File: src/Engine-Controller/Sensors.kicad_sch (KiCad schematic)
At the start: 28 parts, among them P16 647676-2, P17 0530470410, P8 20021511-00026T4LF, U12 MAX4617EUE+T, U13 MAX4617EUE+T, U14 MCP96L01T-E_MX, U15 AD623ARZ-R7, U7 MC74HC4066ADG, U8 AD623ARZ-R7, U9 MC74HC4066ADG

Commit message: resolved all ERC schematic issues
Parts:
- C32: footprint (none) -> Engine-Controller:CAP_0603
- P16: footprint CONN_2043-1X04G00DAU_OUP -> Engine-Controller:647676-2
- P17: footprint CONN_4840.2201_SCH -> Engine-Controller:0530470410
- P8: footprint CONN20_D10-RA-BK_SUL -> Engine-Controller:20021511-00026T4LF
- R19, R20, R21, R22, R23, R24, R25, R26, R27, R29, R30, R31, R32: footprint (none) -> Engine-Controller:RES_0603
- R33: footprint (none) -> Engine-Controller:RES_0805
- U12, U13: footprint (none) -> Engine-Controller:max4617eue
- U14: footprint (none) -> Engine-Controller:MCP96L01T-E_MX
- U15, U8: footprint R_8_ADI -> Engine-Controller:AD623ARZ-R7
- U7, U9: footprint (none) -> Engine-Controller:MC74HC4066ADG
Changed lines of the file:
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@@
       (effects (font (size 1.27 1.27)) (justify right))
     )
-    (property "Footprint" "" (id 2) (at 205.105 52.705 0)
+    (property "Footprint" "Engine-Controller:RES_0603" (id 2) (at 205.105 52.705 0)
       (effects (font (size 1.27 1.27)) (justify left bottom) hide)
     )
@@
       (effects (font (size 1.27 1.27)) hide)
     )
-    (property "Footprint" "" (id 2) (at 259.715 40.64 0)
+    (property "Footprint" "Engine-Controller:MC74HC4066ADG" (id 2) (at 259.715 40.64 0)
       (effects (font (size 1.27 1.27)) hide)
     )
@@
       (effects (font (size 1.27 1.27)) (justify right))
     )
-    (property "Footprint" "" (id 2) (at 276.86 52.07 0)
+    (property "Footprint" "Engine-Controller:RES_0603" (id 2) (at 276.86 52.07 0)
       (effects (font (size 1.27 1.27)) (justify left bottom) hide)
     )
@@
       (effects (font (size 1.524 1.524)) hide)
     )
-    (property "Footprint" "CONN20_D10-RA-BK_SUL" (id 2) (at 16.002 37.973 0)
+    (property "Footprint" "Engine-Controller:20021511-00026T4LF" (id 2) (at 16.002 37.973 0)
       (effects (font (size 1.524 1.524)) hide)
     )
@@
       (effects (font (size 1.27 1.27)) (justify right))
     )
-    (property "Footprint" "" (id 2) (at 266.7 52.07 0)
+    (property "Footprint" "Engine-Controller:RES_0603" (id 2) (at 266.7 52.07 0)
       (effects (font (size 1.27 1.27)) (justify left bottom) hide)
     )
@@
       (effects (font (size 1.27 1.27)) hide)
     )
-    (property "Footprint" "" (id 2) (at 213.995 63.5 0)
+    (property "Footprint" "Engine-Controller:MC74HC4066ADG" (id 2) (at 213.995 63.5 0)
       (effects (font (size 1.27 1.27)) hide)
     )
@@
     (property "Reference" "R33" (id 0) (at 231.775 129.54 0))
     (property "Value" "470" (id 1) (at 236.855 129.54 0))
-    (property "Footprint" "" (id 2) (at 236.22 144.78 0)
+    (property "Footprint" "Engine-Controller:RES_0805" (id 2) (at 236.22 144.78 0)
       (effects (font (size 1.27 1.27)) (justify left bottom) hide)
     )
@@
     )
     (property "Value" "MCP96L01T-E_MX" (id 1) (at 89.535 163.195 0))
-    (property "Footprint" "" (id 2) (at 83.185 172.72 0)
+    (property "Footprint" "Engine-Controller:MCP96L01T-E_MX" (id 2) (at 83.185 172.72 0)
       (effects (font (size 1.27 1.27)) hide)
     )
@@
       (effects (font (size 1.27 1.27)) hide)
     )
-    (property "Footprint" "" (id 2) (at 181.61 63.5 0)
+    (property "Footprint" "Engine-Controller:MC74HC4066ADG" (id 2) (at 181.61 63.5 0)
       (effects (font (size 1.27 1.27)) hide)
     )
@@
       (effects (font (size 1.27 1.27)) (justify right))
     )
-    (property "Footprint" "" (id 2) (at 244.475 52.07 0)
+    (property "Footprint" "Engine-Controller:RES_0603" (id 2) (at 244.475 52.07 0)
       (effects (font (size 1.27 1.27)) (justify left bottom) hide)
     )
@@
       (effects (font (size 1.524 1.524)) hide)
     )
-    (property "Footprint" "R_8_ADI" (id 2) (at 234.696 132.842 0)
+    (property "Footprint" "Engine-Controller:AD623ARZ-R7" (id 2) (at 234.696 132.842 0)
       (effects (font (size 1.524 1.524)) hide)
     )
@@
       (effects (font (size 1.27 1.27)) (justify right))
     )
-    (property "Footprint" "" (id 2) (at 194.31 52.07 0)
+    (property "Footprint" "Engine-Controller:RES_0603" (id 2) (at 194.31 52.07 0)
       (effects (font (size 1.27 1.27)) (justify left bottom) hide)
     )
@@
       (effects (font (size 1.27 1.27)) hide)
     )
-    (property "Footprint" "" (id 2) (at 132.969 39.243 0)
+    (property "Footprint" "Engine-Controller:max4617eue" (id 2) (at 132.969 39.243 0)
       (effects (font (size 1.27 1.27)) hide)
     )
@@
     (property "Reference" "R32" (id 0) (at 60.325 165.1 90))
     (property "Value" "2k" (id 1) (at 59.69 167.005 90))
-    (property "Footprint" "" (id 2) (at 44.45 167.64 0)
+    (property "Footprint" "Engine-Controller:RES_0603" (id 2) (at 44.45 167.64 0)
       (effects (font (size 1.27 1.27)) (justify left bottom) hide)
     )
@@
       (effects (font (size 1.27 1.27)) (justify right))
     )
-    (property "Footprint" "" (id 2) (at 255.27 52.07 0)
+    (property "Footprint" "Engine-Controller:RES_0603" (id 2) (at 255.27 52.07 0)
       (effects (font (size 1.27 1.27)) (justify left bottom) hide)
     )
@@
     (property "Reference" "R31" (id 0) (at 53.975 165.1 90))
     (property "Value" "2k" (id 1) (at 53.34 167.005 90))
-    (property "Footprint" "" (id 2) (at 38.1 167.64 0)
+    (property "Footprint" "Engine-Controller:RES_0603" (id 2) (at 38.1 167.64 0)
       (effects (font (size 1.27 1.27)) (justify left bottom) hide)
     )
@@
       (effects (font (size 1.27 1.27)) hide)
     )
-    (property "Footprint" "" (id 2) (at 203.2 63.5 0)
+    (property "Footprint" "Engine-Controller:MC74HC4066ADG" (id 2) (at 203.2 63.5 0)
       (effects (font (size 1.27 1.27)) hide)
     )
@@
       (effects (font (size 1.27 1.27)) (justify right))
     )
-    (property "Footprint" "" (id 2) (at 226.695 52.07 0)
+    (property "Footprint" "Engine-Controller:RES_0603" (id 2) (at 226.695 52.07 0)
       (effects (font (size 1.27 1.27)) (justify left bottom) hide)
     )
@@
       (effects (font (size 1.27 1.27)) (justify right))
     )
-    (property "Footprint" "" (id 2) (at 285.115 59.055 0)
+    (property "Footprint" "Engine-Controller:RES_0603" (id 2) (at 285.115 59.055 0)
       (effects (font (size 1.27 1.27)) (justify left bottom) hide)
     )
@@
       (effects (font (size 1.27 1.27)) hide)
     )
-    (property "Footprint" "" (id 2) (at 259.715 30.48 0)
+    (property "Footprint" "Engine-Controller:MC74HC4066ADG" (id 2) (at 259.715 30.48 0)
       (effects (font (size 1.27 1.27)) hide)
     )
@@
     (property "Reference" "R29" (id 0) (at 107.315 136.525 0))
     (property "Value" "1M" (id 1) (at 107.315 139.065 0))
-    (property "Footprint" "" (id 2) (at 106.045 121.285 0)
+    (property "Footprint" "Engine-Controller:RES_0603" (id 2) (at 106.045 121.285 0)
       (effects (font (size 1.27 1.27)) (justify left bottom) hide)
     )
@@
       (effects (font (size 1.27 1.27)) hide)
     )
-    (property "Footprint" "" (id 2) (at 254 63.5 0)
+    (property "Footprint" "Engine-Controller:MC74HC4066ADG" (id 2) (at 254 63.5 0)
       (effects (font (size 1.27 1.27)) hide)
     )
@@
       (effects (font (size 1.27 1.27)) hide)
     )
-    (property "Footprint" "" (id 2) (at 132.334 83.058 0)
+    (property "Footprint" "Engine-Controller:max4617eue" (id 2) (at 132.334 83.058 0)
       (effects (font (size 1.27 1.27)) hide)
     )
@@
       (effects (font (size 1.27 1.27)) (justify right))
     )
-    (property "Footprint" "" (id 2) (at 215.9 52.705 0)
+    (property "Footprint" "Engine-Controller:RES_0603" (id 2) (at 215.9 52.705 0)
       (effects (font (size 1.27 1.27)) (justify left bottom) hide)
     )
@@
       (effects (font (size 1.524 1.524)) hide)
     )
-    (property "Footprint" "R_8_ADI" (id 2) (at 223.266 89.027 0)
+    (property "Footprint" "Engine-Controller:AD623ARZ-R7" (id 2) (at 223.266 89.027 0)
       (effects (font (size 1.524 1.524)) hide)
     )
@@
       (effects (font (size 1.27 1.27)) hide)
     )
-    (property "Footprint" "" (id 2) (at 264.16 63.5 0)
+    (property "Footprint" "Engine-Controller:MC74HC4066ADG" (id 2) (at 264.16 63.5 0)
       (effects (font (size 1.27 1.27)) hide)
     )
@@
       (effects (font (size 1.524 1.524)) hide)
     )
-    (property "Footprint" "CONN_4840.2201_SCH" (id 2) (at 201.295 131.445 0)
+    (property "Footprint" "Engine-Controller:0530470410" (id 2) (at 201.295 131.445 0)
       (effects (font (size 1.524 1.524)) hide)
     )
@@
       (effects (font (size 1.27 1.27)) hide)
     )
-    (property "Footprint" "" (id 2) (at 192.405 63.5 0)
+    (property "Footprint" "Engine-Controller:MC74HC4066ADG" (id 2) (at 192.405 63.5 0)
       (effects (font (size 1.27 1.27)) hide)
     )
@@
     (property "Reference" "R30" (id 0) (at 117.475 136.525 0))
     (property "Value" "2M" (id 1) (at 117.475 139.065 0))
-    (property "Footprint" "" (id 2) (at 116.205 121.285 0)
+    (property "Footprint" "Engine-Controller:RES_0603" (id 2) (at 116.205 121.285 0)
       (effects (font (size 1.27 1.27)) (justify left bottom) hide)
     )
@@
       (effects (font (size 1.27 1.27)) (justify left))
     )
-    (property "Footprint" "" (id 2) (at 108.585 160.655 0)
+    (property "Footprint" "Engine-Controller:CAP_0603" (id 2) (at 108.585 160.655 0)
       (effects (font (size 1.27 1.27)) (justify left bottom) hide)
     )
@@
       (effects (font (size 1.27 1.27)) hide)
     )
-    (property "Footprint" "" (id 2) (at 242.57 63.5 0)
+    (property "Footprint" "Engine-Controller:MC74HC4066ADG" (id 2) (at 242.57 63.5 0)
       (effects (font (size 1.27 1.27)) hide)
     )
@@
       (effects (font (size 1.524 1.524)) hide)
     )
-    (property "Footprint" "CONN_2043-1X04G00DAU_OUP" (id 2) (at 137.795 175.26 0)
+    (property "Footprint" "Engine-Controller:647676-2" (id 2) (at 137.795 175.26 0)
       (effects (font (size 1.524 1.524)) hide)
     )
@@
       (effects (font (size 1.27 1.27)) hide)
     )
-    (property "Footprint" "" (id 2) (at 231.775 63.5 0)
-      (effects (font (size 1.27 1.27)) hide)
-    )
+    (property "Footprint" "Engine-Controller:MC74HC4066ADG" (id 2) (at 231.775 63.5 0)
+      (effects (font (size 1.27 1.27)) hide)
+    )

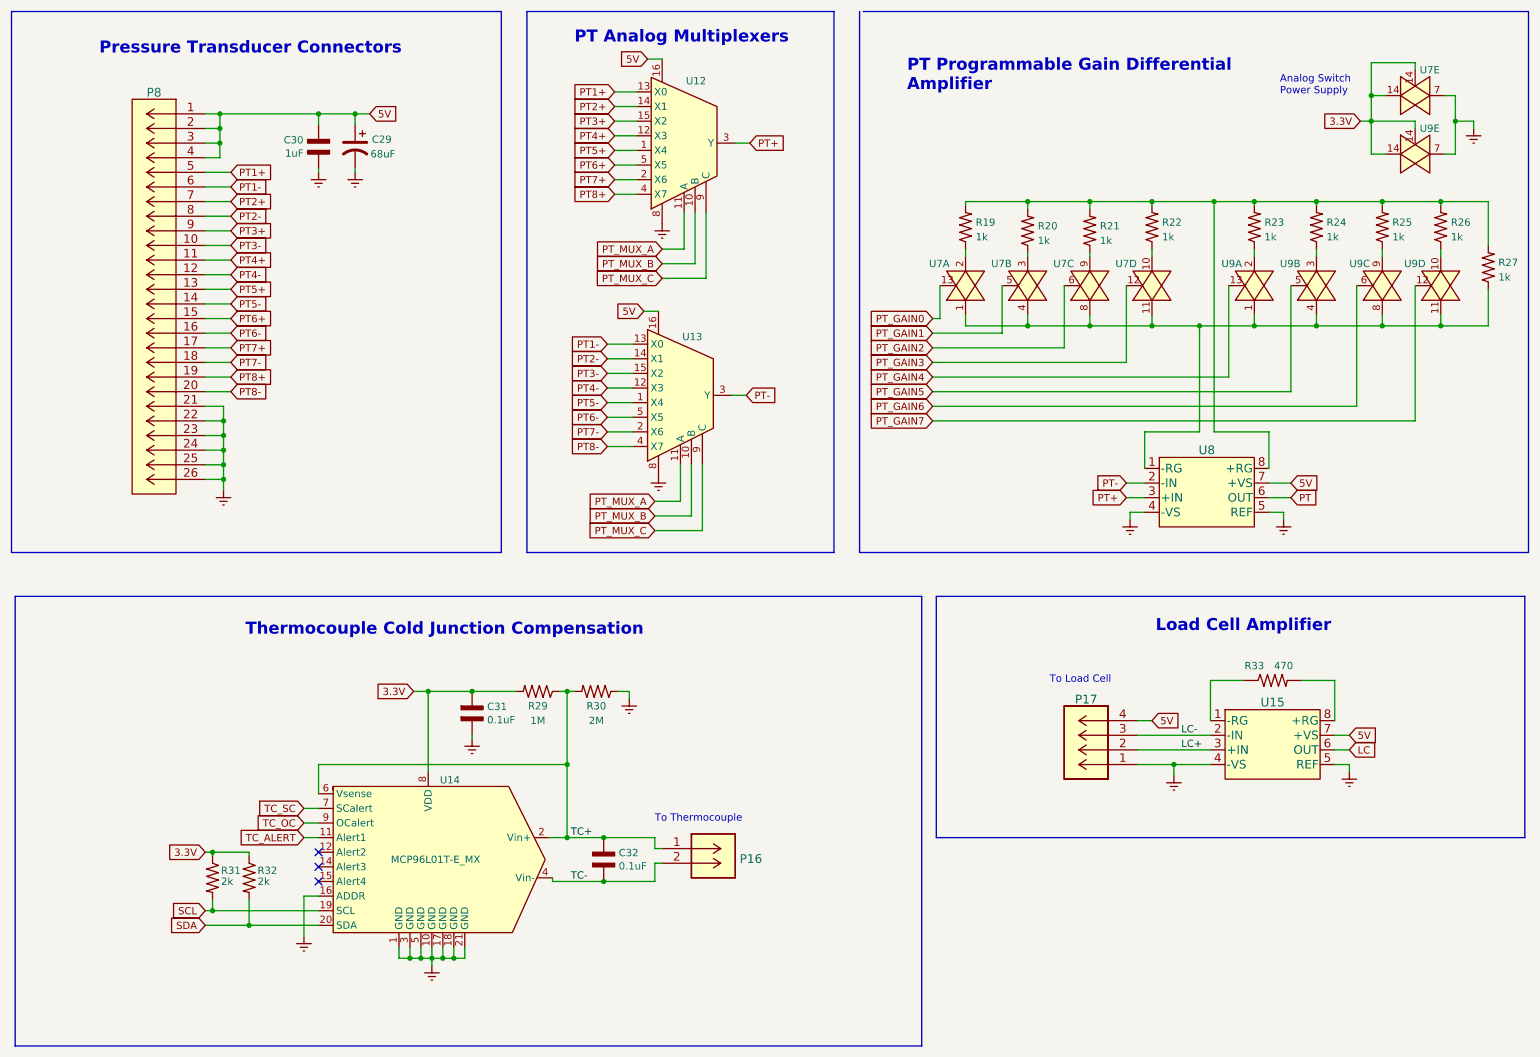
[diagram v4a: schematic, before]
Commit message: added load resistors to amplifier outputs
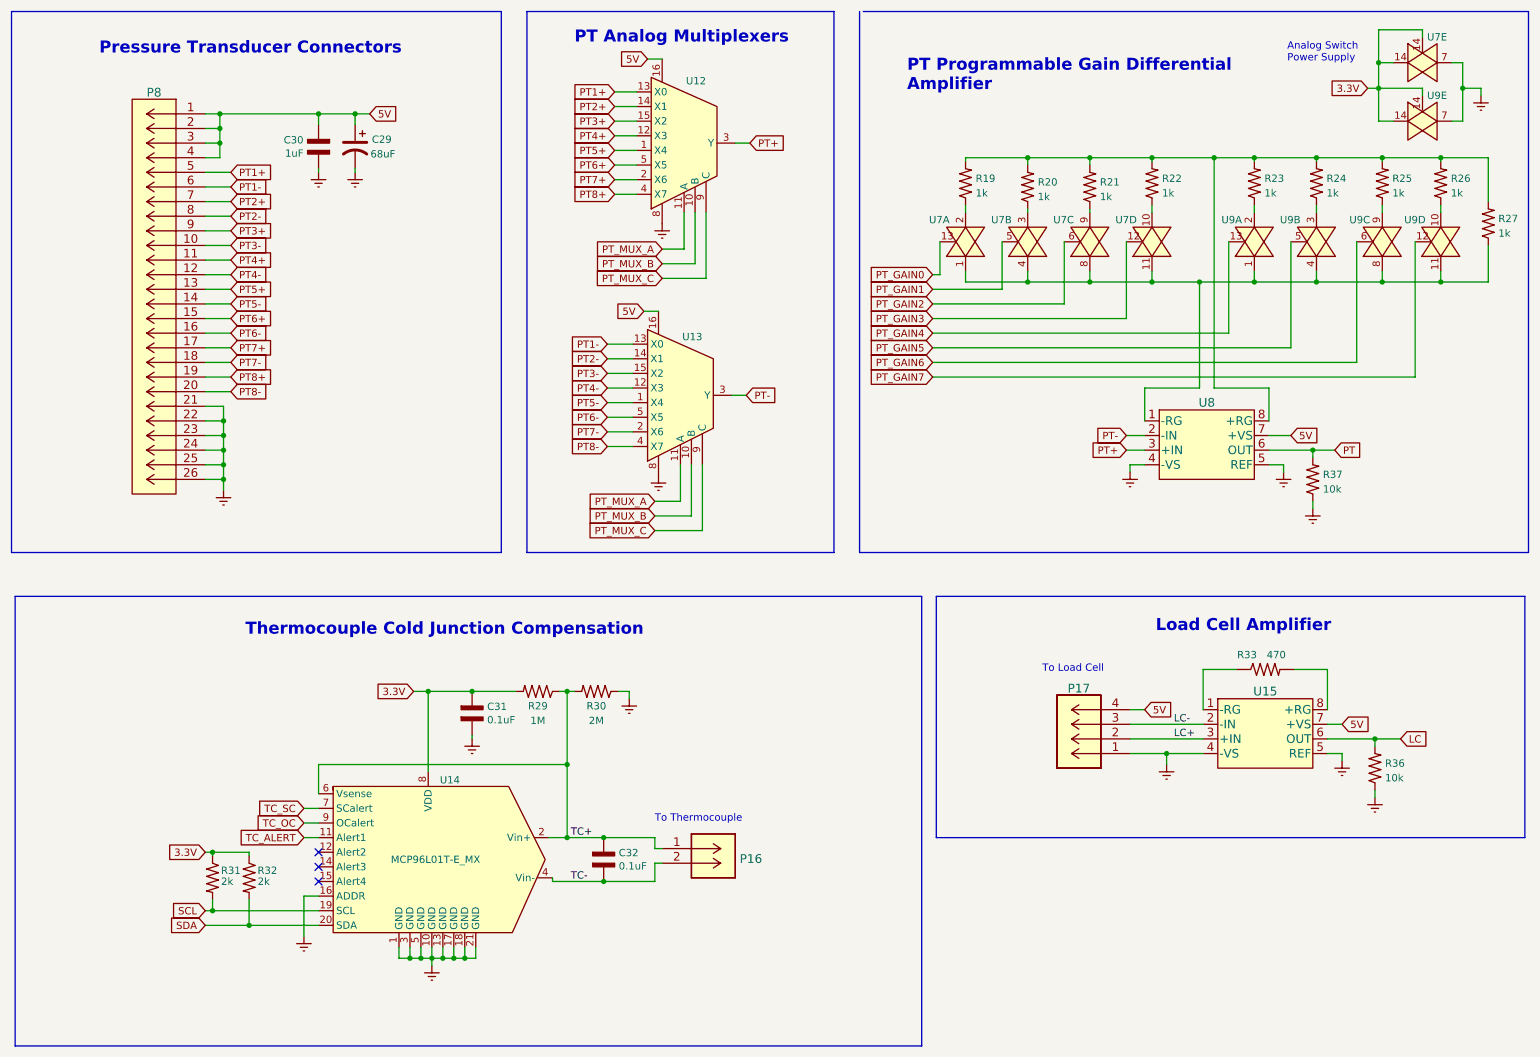
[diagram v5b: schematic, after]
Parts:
- added R36, R37: 10k, Engine-Controller:RES_0603, symbol Engine-Controller:RES_0603
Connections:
- net Earth: now also U14.13 (GND), R36.1, R37.1
- net LC: now also R36.2
- net PT: now also R37.2
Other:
- moved on the sheet: P17, R19, R20, R21, R22, R23, R24, R25, R26, R27, R33, U15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

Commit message: routed rev4
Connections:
- net 3.3V: no longer U7.14, U9.14
- net Earth: now also U12.6 (EN), U13.6 (EN)
- new net A3.3V: U7.14, U9.14
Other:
- moved on the sheet: R20
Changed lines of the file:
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@@
+    (stroke (width 0) (type default) (color 0 0 0 0))
+  )
+  (wire (pts (xy 135.255 71.755) (xy 138.43 71.755))
     (stroke (width 0) (type default) (color 0 0 0 0))
   )
@@
     (stroke (width 0) (type default) (color 0 0 0 0))
   )
+  (wire (pts (xy 135.255 72.39) (xy 135.255 71.755))
+    (stroke (width 0) (type default) (color 0 0 0 0))
+  )
   (wire (pts (xy 203.2 50.165) (xy 203.2 50.8))
     (stroke (width 0) (type default) (color 0 0 0 0))
@@
     (stroke (width 0) (type default) (color 0 0 0 0))
   )
+  (wire (pts (xy 138.43 71.755) (xy 138.43 72.39))
+    (stroke (width 0) (type default) (color 0 0 0 0))
+  )
   (wire (pts (xy 175.895 64.135) (xy 187.96 64.135))
     (stroke (width 0) (type default) (color 0 0 0 0))
@@
     (stroke (width 0) (type default) (color 0 0 0 0))
   )
+  (wire (pts (xy 139.7 27.305) (xy 139.7 28.575))
+    (stroke (width 0) (type default) (color 0 0 0 0))
+  )
   (wire (pts (xy 231.775 60.96) (xy 231.775 62.865))
     (stroke (width 0) (type default) (color 0 0 0 0))
   )
+  (wire (pts (xy 135.89 27.305) (xy 139.7 27.305))
+    (stroke (width 0) (type default) (color 0 0 0 0))
+  )
   (wire (pts (xy 49.53 33.655) (xy 52.07 33.655))
     (stroke (width 0) (type default) (color 0 0 0 0))
@@
   )
   (wire (pts (xy 126.365 24.13) (xy 128.905 24.13))
+    (stroke (width 0) (type default) (color 0 0 0 0))
+  )
+  (wire (pts (xy 135.89 28.575) (xy 135.89 27.305))
     (stroke (width 0) (type default) (color 0 0 0 0))
   )
@@
     )
   )
-  (global_label "3.3V" (shape input) (at 251.46 29.21 180) (fields_autoplaced)
-    (effects (font (size 1.27 1.27)) (justify right))
-    (property "Intersheet References" "${INTERSHEET_REFS}" (id 0) (at 245.0234 29.1306 0)
+  (global_label "A3.3V" (shape input) (at 251.46 29.21 180) (fields_autoplaced)
+    (effects (font (size 1.27 1.27)) (justify right))
+    (property "Intersheet References" "${INTERSHEET_REFS}" (id 0) (at 243.9348 29.1306 0)
       (effects (font (size 1.27 1.27)) (justify right) hide)
     )
@@
     (pin "2")
   )
-  (symbol (lib_id "Engine-Controller:RES_0603") (at 192.405 46.355 90) (unit 1)
+  (symbol (lib_id "Engine-Controller:RES_0603") (at 192.405 46.355 270) (mirror x) (unit 1)
     (in_bom yes) (on_board yes) (fields_autoplaced)
     (property "Reference" "R20" (id 0) (at 194.1576 45.5203 90)
-      (effects (font (size 1.27 1.27)) (justify right))
+      (effects (font (size 1.27 1.27)) (justify left))
     )
     (property "Value" "1k" (id 1) (at 194.1576 48.0572 90)
-      (effects (font (size 1.27 1.27)) (justify right))
-    )
-    (property "Footprint" "Engine-Controller:RES_0603" (id 2) (at 205.105 45.085 0)
+      (effects (font (size 1.27 1.27)) (justify left))
+    )
+    (property "Footprint" "Engine-Controller:RES_0603" (id 2) (at 179.705 45.085 0)
       (effects (font (size 1.27 1.27)) (justify left bottom) hide)
     )
@@
     (pin "2")
   )
-  (symbol (lib_name "MAX4617EUE+T_1") (lib_id "Engine-Controller:MAX4617EUE+T") (at 132.715 38.735 0) (unit 1)
+  (symbol (lib_id "Engine-Controller:MAX4617EUE+T") (at 132.715 38.735 0) (unit 1)
     (in_bom yes) (on_board yes)
-    (property "Reference" "U12" (id 0) (at 136.525 27.94 0)
+    (property "Reference" "U12" (id 0) (at 134.62 27.305 0)
       (effects (font (size 1.27 1.27)) (justify right))
     )
@@
     (pin "4")
     (pin "5")
+    (pin "6")
     (pin "8")
     (pin "9")
@@
     (pin "1")
     (pin "2")
+  )
+  (symbol (lib_id "Engine-Controller:Earth") (at 139.7 28.575 0) (mirror y) (unit 1)
+    (in_bom yes) (on_board yes) (fields_autoplaced)
+    (property "Reference" "#PWR0113" (id 0) (at 139.7 34.925 0)
+      (effects (font (size 1.27 1.27)) hide)
+    )
+    (property "Value" "Earth" (id 1) (at 139.7 32.385 0)
+      (effects (font (size 1.27 1.27)) hide)
+    )
+    (property "Footprint" "" (id 2) (at 139.7 28.575 0)
+      (effects (font (size 1.27 1.27)) hide)
+    )
+    (property "Datasheet" "" (id 3) (at 139.7 28.575 0)
+      (effects (font (size 1.27 1.27)) hide)
+    )
+    (pin "1")
   )
   (symbol (lib_id "Engine-Controller:RES_0603") (at 242.57 45.72 90) (unit 1)
@@
     (pin "7")
   )
+  (symbol (lib_id "Engine-Controller:Earth") (at 138.43 72.39 0) (mirror y) (unit 1)
+    (in_bom yes) (on_board yes) (fields_autoplaced)
+    (property "Reference" "#PWR0112" (id 0) (at 138.43 78.74 0)
+      (effects (font (size 1.27 1.27)) hide)
+    )
+    (property "Value" "Earth" (id 1) (at 138.43 76.2 0)
+      (effects (font (size 1.27 1.27)) hide)
+    )
+    (property "Footprint" "" (id 2) (at 138.43 72.39 0)
+      (effects (font (size 1.27 1.27)) hide)
+    )
+    (property "Datasheet" "" (id 3) (at 138.43 72.39 0)
+      (effects (font (size 1.27 1.27)) hide)
+    )
+    (pin "1")
+  )
   (symbol (lib_id "Engine-Controller:RES_0603") (at 213.995 45.72 90) (unit 1)
     (in_bom yes) (on_board yes) (fields_autoplaced)
@@
   (symbol (lib_id "Engine-Controller:MAX4617EUE+T") (at 132.08 82.55 0) (unit 1)
     (in_bom yes) (on_board yes)
-    (property "Reference" "U13" (id 0) (at 135.89 72.39 0)
+    (property "Reference" "U13" (id 0) (at 133.35 71.12 0)
       (effects (font (size 1.27 1.27)) (justify right))
     )
@@
     (pin "4")
     (pin "5")
+    (pin "6")
     (pin "8")
     (pin "9")
